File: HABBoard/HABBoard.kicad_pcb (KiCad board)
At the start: 4 copper layers, 100 x 100 mm, 212 parts, among them J1 USB_C_MCU, J10 RFShield_TwoPieces, J2 USB_C_GNSS, J3 MEM2067-02-180-00-A_REVB, J4 GPS In, J5 GNSS_UART, J6 DEBUG, J7 VHF Out, J8 UHF Out, J9 RFShield_TwoPieces, Q1 SSM6N7002KFU, Q2 SSM6N7002KFU, Q3 SSM6N7002KFU, Q4 PMN16XNE, SW1 RESET, SW2 BOOT, SW3 USER_BUTTON, SW4 Power, U1 TC2015-3.3VxCTTR, U10 SX1276, U11 SX1276, U12 MP5016GQH-Z, U13 PE42421, U14 ISL91127IR, U15 TPS2116DRLR, U16 INA219BxD, U2 W25Q128JVS, U3 NEO-M9N-00B, U4 AP2138N-2.5, U5 RP2040, U6 BME680, U7 TXS0104E, U8 ICM-20948, U9 AP2138N-1.8, Y1 ECS-TXO-25CSMV-320-BM-TR, Y2 ECS-TXO-25CSMV-320-BM-TR, Y3 12.000MHz

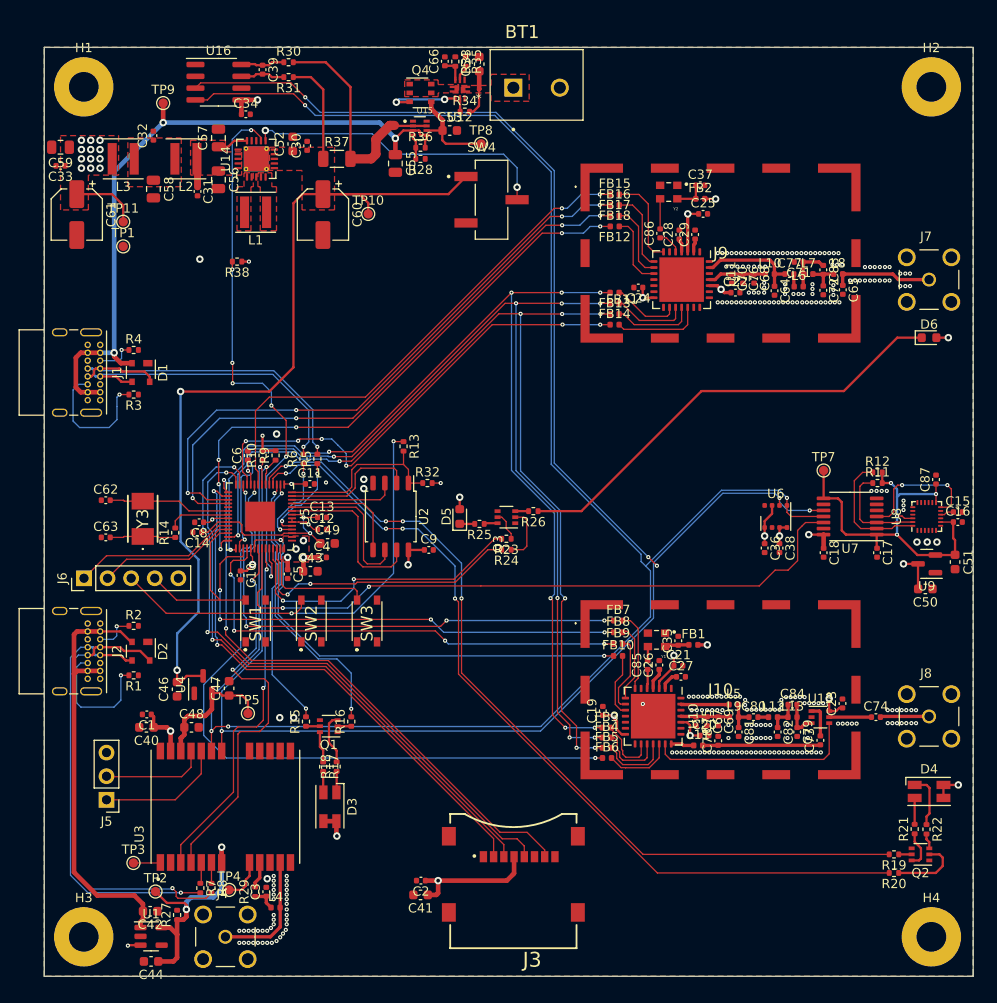
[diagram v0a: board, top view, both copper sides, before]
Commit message: Adjust RF Layout
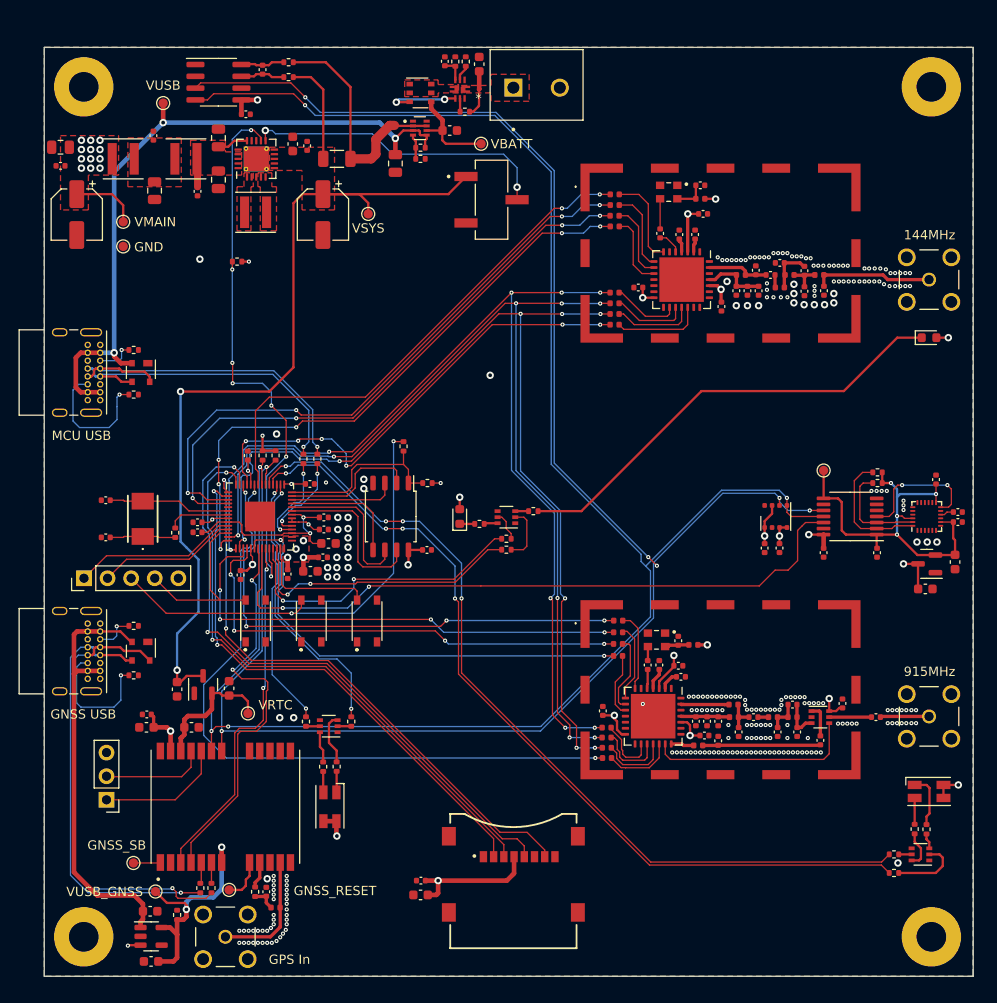
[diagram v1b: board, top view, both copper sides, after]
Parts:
- J1: value USB_C_MCU -> MCU USB
- J2: value USB_C_GNSS -> GNSS USB
- J7: value VHF Out -> 144MHz
- J8: value UHF Out -> 915MHz
- moved L10 3.12 mm to (102.8, 49.5)
- moved C64 2.98 mm to (104.3, 49.0), turned to 90 degrees
- moved C22 2.13 mm to (100.7, 52.9), turned to -90 degrees
- moved C65 2.03 mm to (111.7, 51.2)
- moved C71 2.03 mm to (106.9, 48.2)
- moved C72 2.03 mm to (109.6, 51.2)
- moved C77 2.03 mm to (105.9, 49.5)
- moved C83 2.03 mm to (109.6, 49.0)
- moved L6 2.03 mm to (106.9, 50.9)
- moved L7 2.03 mm to (108.0, 49.5)
- moved L8 2.03 mm to (111.2, 49.5)
- moved C68 1.39 mm to (104.7, 51.2)
- moved C70 1.39 mm to (102.2, 51.2)
- moved C76 1.39 mm to (103.5, 51.2)
- moved C58 0.22 mm to (39.6, 40.4)
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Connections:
- J1 pad S1: unconnected-(J1-PadS1) -> (no net)
- J2 pad S1: unconnected-(J2-PadS1) -> (no net)
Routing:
- net Net-(C64-Pad1): track 11.0 -> 6.86 mm
- net Net-(C65-Pad1): track 10.8 -> 12.8 mm
- net +3V3: track 108.7 -> 109.5 mm
- net +1V1: track 19.8 -> 20.6 mm
- net /UHF_SRED: track 92.6 -> 93.2 mm
- net Net-(C68-Pad1): track 6.28 -> 6.83 mm
- net GND: vias 273 -> 260
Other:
- rule pad_to_mask_clearance: 0.1 -> 0

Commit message: rearranged RF and more Via stitching
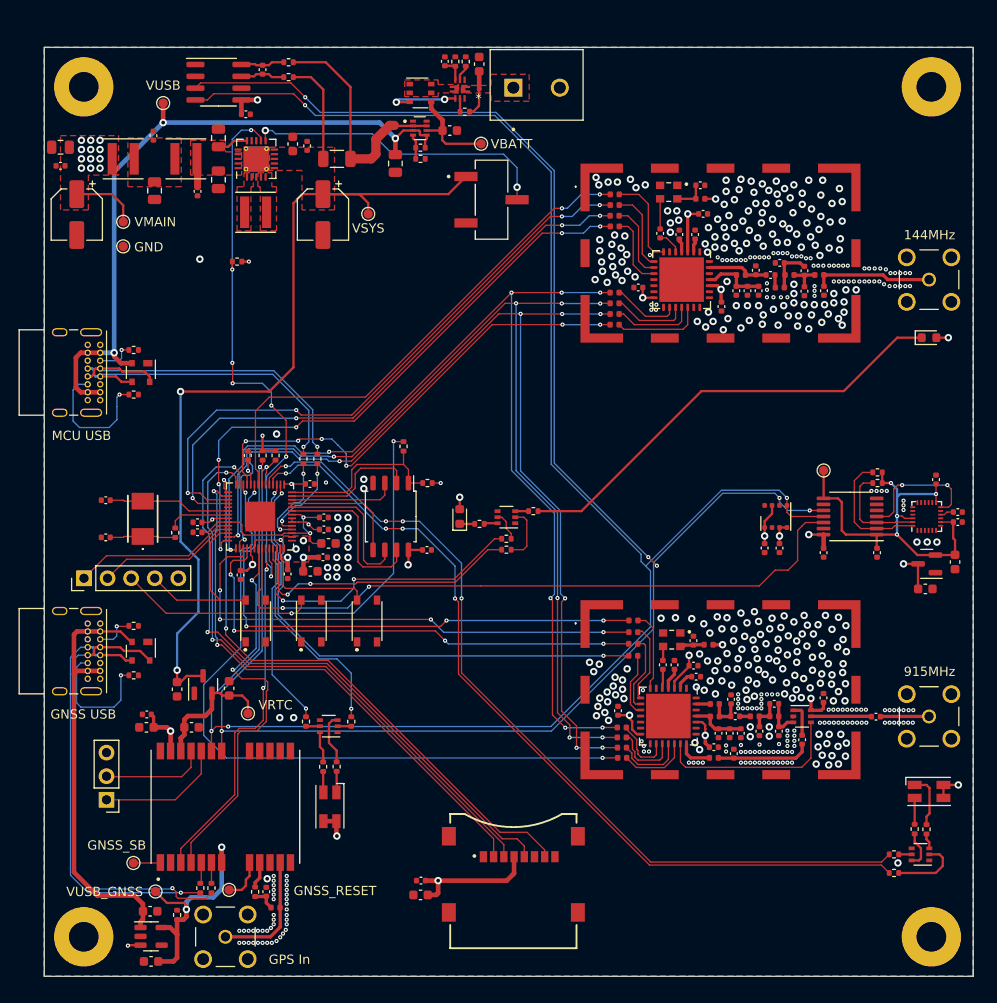
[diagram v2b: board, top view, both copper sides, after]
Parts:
- moved C81 3.61 mm to (101.7, 95.2), turned to 90 degrees
- moved C67 2.75 mm to (101.5, 98.8)
- moved C69 2.75 mm to (102.7, 98.8)
- moved C75 2.75 mm to (100.3, 98.8)
- moved C78 2.18 mm to (102.0, 101.0)
- moved L11 2.15 mm to (99.8, 101.5)
- moved C23 2.13 mm to (111.6, 95.0)
- moved L9 2.07 mm to (99.9, 97.0)
- moved L5 2.02 mm to (99.9, 95.7)
- moved C79 1.97 mm to (106.8, 98.6)
- moved C82 1.97 mm to (104.7, 98.6)
- moved C84 1.97 mm to (106.3, 95.7)
- moved L12 1.97 mm to (104.2, 97.0)
- moved L13 1.97 mm to (106.3, 97.0)
- moved U13 1.97 mm to (109.3, 97.0)
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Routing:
- net Net-(L5-Pad1): track 5.20 -> 1.53 mm
- net Net-(C73-Pad1): track 12.7 -> 10.1 mm
- net Net-(U10-Pad20): track 22.5 -> 20.5 mm
- net Net-(C74-Pad1): track 4.55 -> 6.53 mm
- net /UHF_DIO1: track 51.9 -> 53.6 mm
- net /UHF_DIO2: track 50.1 -> 51.8 mm
- net /UHF_DIO0: track 52.6 -> 54.2 mm
- net /UHF_NSS: track 73.8 -> 75.5 mm
- net /RF_SCK: track 112.8 -> 114.5 mm
- net /RF_MOSI: track 110.0 -> 111.7 mm
- net /RF_MISO: track 109.7 -> 111.3 mm
- net /UHF_RESET: track 56.6 -> 58.2 mm
- net Net-(L11-Pad1): track 2.48 -> 3.71 mm
- net +3V3: track 109.5 -> 110.4 mm
- net /BME_SDA: track 206.9 -> 207.6 mm
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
